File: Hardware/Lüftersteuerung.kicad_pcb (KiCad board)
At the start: 2 copper layers, 65 x 74 mm, 70 parts, among them J1 CH0, J2 CH1, J3 CH2, J4 CH3, J5 CH4, J6 CH5, P1 ISP_HEADER, P5 I2C_DEBUG, P6 SPI_DEBUG, SW1 SW_NB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

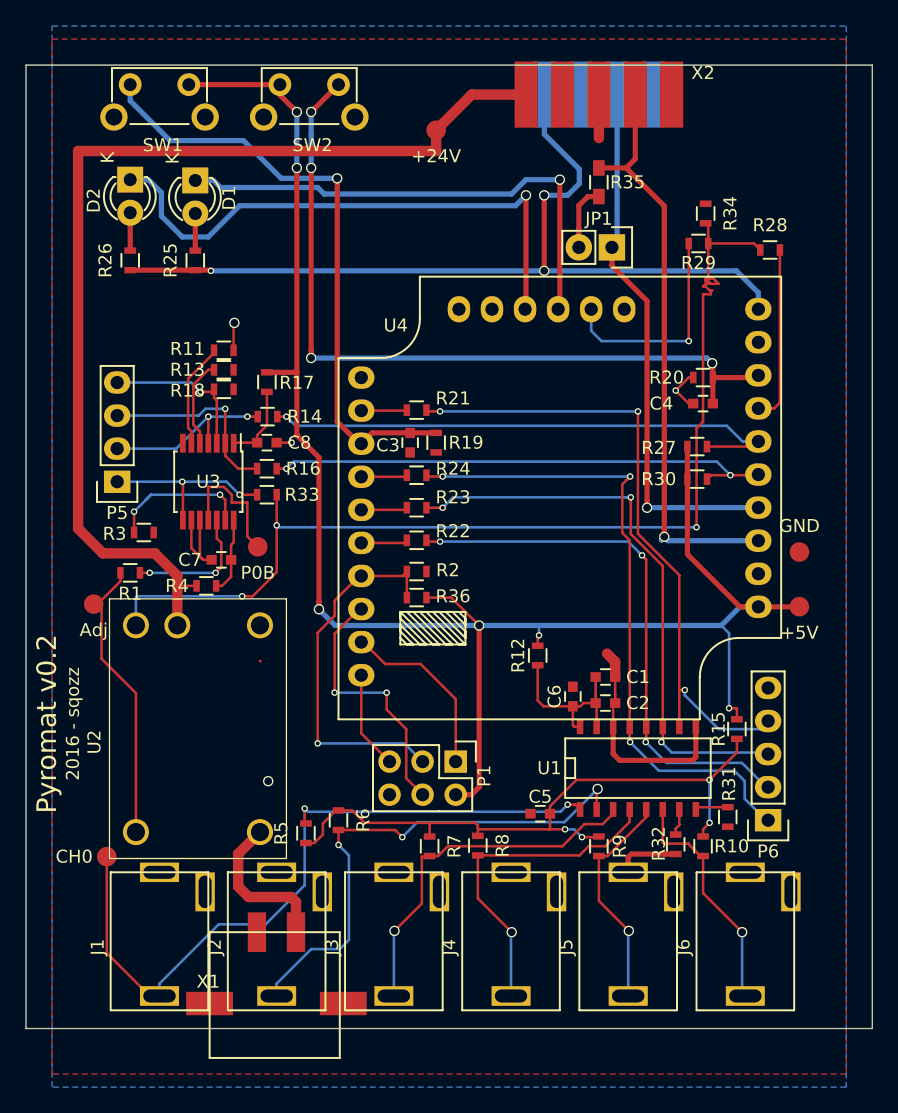
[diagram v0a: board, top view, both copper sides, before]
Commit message: fixed all known hardware issues
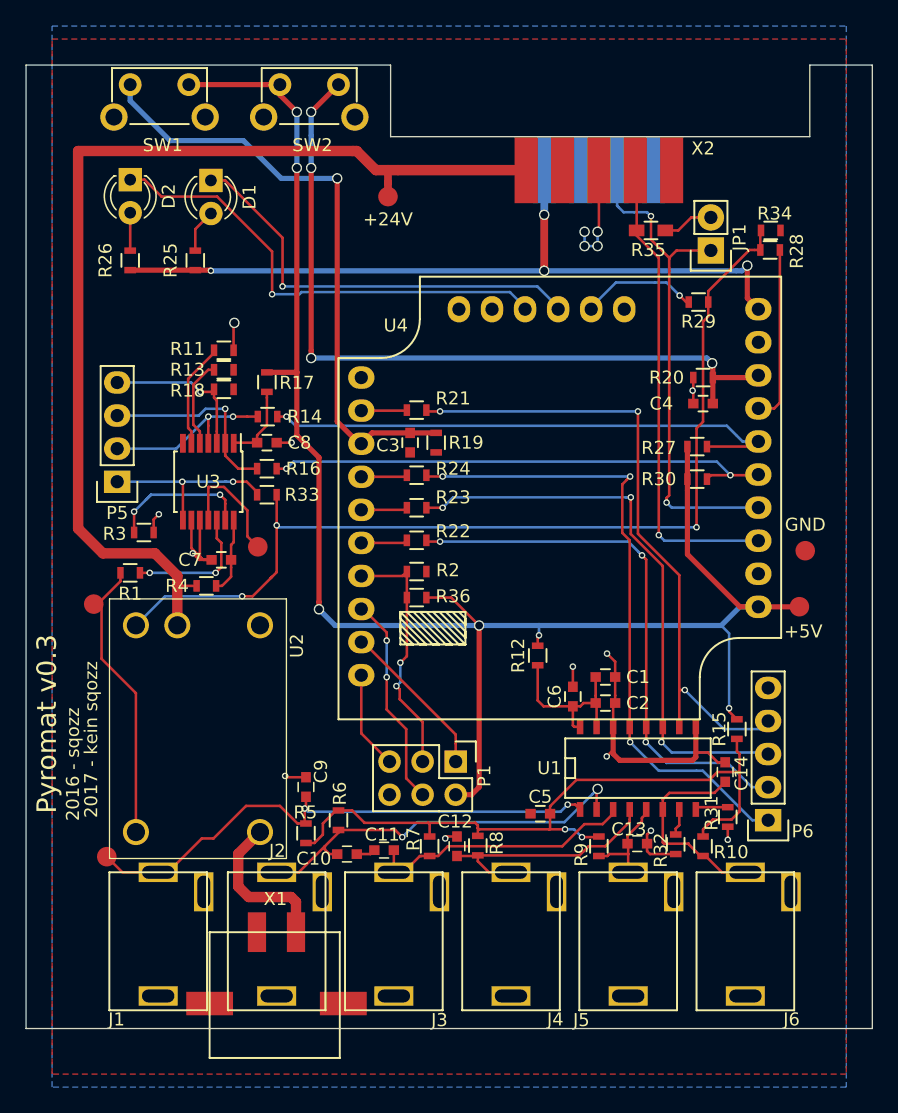
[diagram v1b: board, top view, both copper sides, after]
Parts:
- removed W8: +24V, Measurement_Points:Measurement_Point_Round-SMD-Pad_Small
- added +24V: TEST_1P, Measurement_Points:Measurement_Point_Round-SMD-Pad_Small, F.Cu at (52.8, 103.6)
- added C10: 10nF, Capacitors_SMD:C_0603, F.Cu at (49.6, 154.1)
- added C11: 10nF, Capacitors_SMD:C_0603, F.Cu at (52.5, 153.8)
- added C12: 10nF, Capacitors_SMD:C_0603, F.Cu at (58.1, 153.5)
- added C13: 10nF, Capacitors_SMD:C_0603, F.Cu at (72.0, 153.3)
- added C14: 10nF, Capacitors_SMD:C_0603, F.Cu at (78.7, 147.8)
- added C9: 10nF, Capacitors_SMD:C_0603, F.Cu at (46.5, 148.9)
- D1, D2: footprint LEDs:LED-3MM -> LEDs:LED_D3.0mm
- W10: value P0B -> TEST_1P
- W12: value CH0 -> TEST_1P
- W9: value Adj -> TEST_1P
- moved JP1 7.60 mm to (77.6, 107.7), turned to 180 degrees
- moved X2 5.80 mm to (69.0, 98.9)
- moved R35 5.45 mm to (73.0, 106.2), turned to 0 degrees
- moved R34 5.17 mm to (82.2, 106.2), turned to 180 degrees
- moved R29 4.50 mm to (76.7, 111.7)
- moved D1 1.20 mm to (39.2, 102.4)
- moved GND 0.46 mm to (84.8, 130.8)
- moved J1 0.10 mm to (38.9, 155.5)
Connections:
- J1 pad 1: /Sensoren/CH0 -> GND
- J1 pad 2: GND -> /Sensoren/CH0
- J1 pad 3: Net-(J1-Pad3) -> (no net)
- J2 pad 1: /Sensoren/CH1 -> GND
- J2 pad 2: GND -> /Sensoren/CH1
- J2 pad 3: Net-(J2-Pad3) -> (no net)
- J3 pad 1: /Sensoren/CH2 -> GND
- J3 pad 2: GND -> /Sensoren/CH2
- J3 pad 3: Net-(J3-Pad3) -> (no net)
- J4 pad 1: /Sensoren/CH3 -> GND
- J4 pad 2: GND -> /Sensoren/CH3
- J4 pad 3: Net-(J4-Pad3) -> (no net)
- J5 pad 1: /Sensoren/CH4 -> GND
- J5 pad 2: GND -> /Sensoren/CH4
- J5 pad 3: Net-(J5-Pad3) -> (no net)
- J6 pad 1: /Sensoren/CH5 -> GND
- J6 pad 2: GND -> /Sensoren/CH5
- J6 pad 3: Net-(J6-Pad3) -> (no net)
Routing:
- net GND: track 39.1 -> 56.7 mm, vias 3 -> 16
- net /Sensoren/CH0: track 56.8 -> 42.2 mm
- net /Sensoren/CH4: track 17.5 -> 7.75 mm, vias 1 -> 0
- net /Sensoren/CH1: track 39.9 -> 30.8 mm, vias 3 -> 2
- net Net-(P1-Pad3): track 28.6 -> 19.6 mm, vias 1 -> 2
- net Net-(R35-Pad1): track 45.3 -> 36.6 mm
- net Net-(R29-Pad2): track 17.0 -> 9.05 mm
- net +12V: track 67.1 -> 59.2 mm, vias 3 -> 4
- net /Lüftersteuerung/~FAN_Enable: track 83.8 -> 76.3 mm
- net /Sensoren/CH2: track 28.0 -> 20.8 mm, vias 1 -> 0
- net /Sensoren/CH3: track 25.6 -> 18.7 mm, vias 1 -> 0
- net Net-(D2-Pad1): track 43.4 -> 36.7 mm
- net Net-(D1-Pad1): track 39.0 -> 33.2 mm
- net Net-(P1-Pad4): track 20.3 -> 16.5 mm
- net Net-(C5-Pad2): track 50.2 -> 53.9 mm, vias 4 -> 2
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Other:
- outline, holes or cut-outs redrawn
- board text added: "2017 - kein sqozz"
- board text added: "Pyromat v0.3"
- board text removed: "Pyromat v0.2"
